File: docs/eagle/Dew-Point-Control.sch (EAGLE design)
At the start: 5 parts

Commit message: updated eagle board and schematic
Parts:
- added RELAYS: (no value), pinhead:PINHD-1X6
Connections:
- new net GPIO17: RELAYS.5, RPI_GPIO.11
- new net GPIO22: RELAYS.3, RPI_GPIO.15
- new net GPIO24: RELAYS.2, RPI_GPIO.18
- new net GPIO27: RELAYS.4, RPI_GPIO.13
- net 5V: now also RELAYS.6
- net GND: now also RELAYS.1
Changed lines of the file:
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@@
 <part name="R1" library="rcl" deviceset="R-EU_" device="0207/10" value="4,7K"/>
 <part name="R2" library="rcl" deviceset="R-EU_" device="0207/10" value="4,7K"/>
+<part name="RELAYS" library="pinhead" deviceset="PINHD-1X6" device=""/>
 </parts>
 <sheets>
@@
 <instance part="R1" gate="G$1" x="38.1" y="76.2" rot="R90"/>
 <instance part="R2" gate="G$1" x="63.5" y="76.2" rot="R90"/>
+<instance part="RELAYS" gate="A" x="83.82" y="48.26"/>
 </instances>
 <busses>
@@
 <wire x1="43.18" y1="83.82" x2="43.18" y2="73.66" width="0.1524" layer="91"/>
 <pinref part="SENSOR1" gate="A" pin="1"/>
-<wire x1="43.18" y1="73.66" x2="53.34" y2="73.66" width="0.1524" layer="91"/>
+<wire x1="43.18" y1="73.66" x2="45.72" y2="73.66" width="0.1524" layer="91"/>
+<wire x1="45.72" y1="73.66" x2="53.34" y2="73.66" width="0.1524" layer="91"/>
 <wire x1="43.18" y1="83.82" x2="63.5" y2="83.82" width="0.1524" layer="91"/>
 <wire x1="63.5" y1="83.82" x2="68.58" y2="83.82" width="0.1524" layer="91"/>
@@
 <junction x="43.18" y="83.82"/>
 <junction x="63.5" y="83.82"/>
+<wire x1="45.72" y1="73.66" x2="45.72" y2="43.18" width="0.1524" layer="91"/>
+<junction x="45.72" y="73.66"/>
+<pinref part="RELAYS" gate="A" pin="6"/>
+<wire x1="81.28" y1="43.18" x2="45.72" y2="43.18" width="0.1524" layer="91"/>
+<label x="71.12" y="43.18" size="1.778" layer="95"/>
 </segment>
 </net>
@@
 <label x="25.4" y="68.58" size="1.778" layer="95"/>
 <junction x="43.18" y="68.58"/>
+<wire x1="68.58" y1="60.96" x2="68.58" y2="55.88" width="0.1524" layer="91"/>
+<pinref part="RELAYS" gate="A" pin="1"/>
+<wire x1="68.58" y1="55.88" x2="81.28" y2="55.88" width="0.1524" layer="91"/>
+<junction x="68.58" y="60.96"/>
+<label x="71.12" y="55.88" size="1.778" layer="95"/>
 </segment>
 </net>
@@
 </segment>
 </net>
+<net name="GPIO24" class="0">
+<segment>
+<pinref part="RPI_GPIO" gate="A" pin="18"/>
+<label x="25.4" y="53.34" size="1.778" layer="95"/>
+<wire x1="20.32" y1="53.34" x2="81.28" y2="53.34" width="0.1524" layer="91"/>
+<pinref part="RELAYS" gate="A" pin="2"/>
+<label x="66.04" y="53.34" size="1.778" layer="95"/>
+</segment>
+</net>
+<net name="GPIO17" class="0">
+<segment>
+<pinref part="RPI_GPIO" gate="A" pin="11"/>
+<wire x1="12.7" y1="60.96" x2="-10.16" y2="60.96" width="0.1524" layer="91"/>
+<label x="-2.54" y="60.96" size="1.778" layer="95"/>
+<wire x1="-10.16" y1="60.96" x2="-10.16" y2="40.64" width="0.1524" layer="91"/>
+<wire x1="-10.16" y1="40.64" x2="38.1" y2="40.64" width="0.1524" layer="91"/>
+<wire x1="38.1" y1="40.64" x2="38.1" y2="45.72" width="0.1524" layer="91"/>
+<pinref part="RELAYS" gate="A" pin="5"/>
+<wire x1="38.1" y1="45.72" x2="81.28" y2="45.72" width="0.1524" layer="91"/>
+<label x="66.04" y="45.72" size="1.778" layer="95"/>
+</segment>
+</net>
+<net name="GPIO27" class="0">
+<segment>
+<pinref part="RPI_GPIO" gate="A" pin="13"/>
+<wire x1="12.7" y1="58.42" x2="-7.62" y2="58.42" width="0.1524" layer="91"/>
+<label x="-2.54" y="58.42" size="1.778" layer="95"/>
+<wire x1="-7.62" y1="58.42" x2="-7.62" y2="43.18" width="0.1524" layer="91"/>
+<wire x1="-7.62" y1="43.18" x2="35.56" y2="43.18" width="0.1524" layer="91"/>
+<wire x1="35.56" y1="43.18" x2="35.56" y2="48.26" width="0.1524" layer="91"/>
+<pinref part="RELAYS" gate="A" pin="4"/>
+<wire x1="35.56" y1="48.26" x2="81.28" y2="48.26" width="0.1524" layer="91"/>
+<label x="66.04" y="48.26" size="1.778" layer="95"/>
+</segment>
+</net>
+<net name="GPIO22" class="0">
+<segment>
+<pinref part="RPI_GPIO" gate="A" pin="15"/>
+<wire x1="12.7" y1="55.88" x2="-5.08" y2="55.88" width="0.1524" layer="91"/>
+<label x="-2.54" y="55.88" size="1.778" layer="95"/>
+<wire x1="-5.08" y1="55.88" x2="-5.08" y2="45.72" width="0.1524" layer="91"/>
+<wire x1="-5.08" y1="45.72" x2="33.02" y2="45.72" width="0.1524" layer="91"/>
+<wire x1="33.02" y1="45.72" x2="33.02" y2="50.8" width="0.1524" layer="91"/>
+<pinref part="RELAYS" gate="A" pin="3"/>
+<wire x1="33.02" y1="50.8" x2="81.28" y2="50.8" width="0.1524" layer="91"/>
+<label x="66.04" y="50.8" size="1.778" layer="95"/>
+</segment>
+</net>

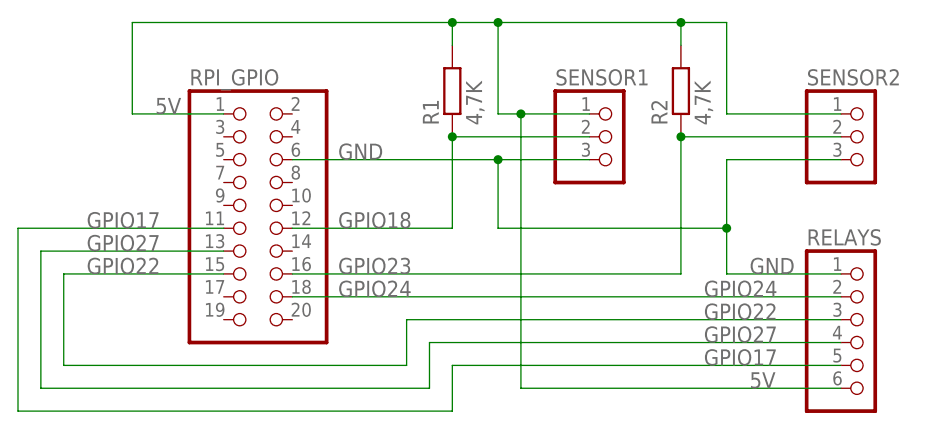
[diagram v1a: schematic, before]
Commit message: rename project and add init script
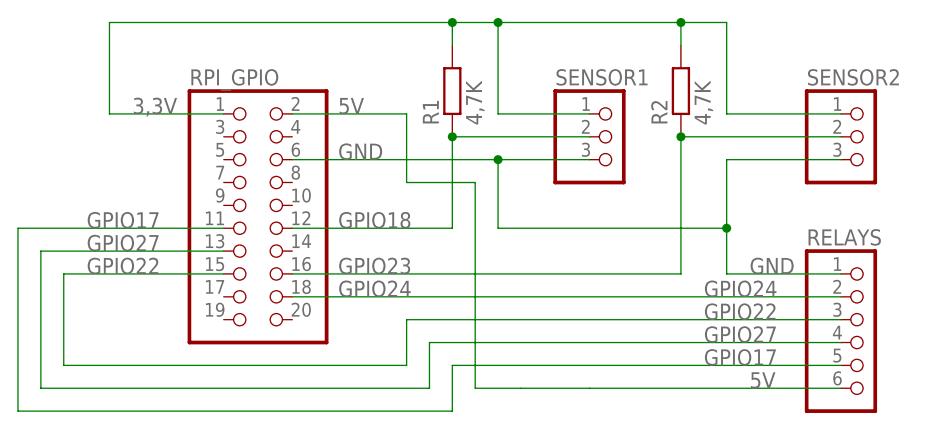
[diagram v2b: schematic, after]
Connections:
- new net 3,3V: R1.2, R2.2, RPI_GPIO.1, SENSOR1.1, SENSOR2.1
- net 5V: now also RPI_GPIO.2; no longer R1.2, R2.2, RPI_GPIO.1, SENSOR1.1, SENSOR2.1
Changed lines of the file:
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@@
 </busses>
 <nets>
-<net name="5V" class="0">
+<net name="3,3V" class="0">
 <segment>
 <pinref part="RPI_GPIO" gate="A" pin="1"/>
-<wire x1="12.7" y1="73.66" x2="2.54" y2="73.66" width="0.1524" layer="91"/>
-<wire x1="2.54" y1="73.66" x2="2.54" y2="83.82" width="0.1524" layer="91"/>
-<wire x1="2.54" y1="83.82" x2="38.1" y2="83.82" width="0.1524" layer="91"/>
+<wire x1="12.7" y1="73.66" x2="0" y2="73.66" width="0.1524" layer="91"/>
+<wire x1="0" y1="73.66" x2="0" y2="83.82" width="0.1524" layer="91"/>
+<wire x1="0" y1="83.82" x2="38.1" y2="83.82" width="0.1524" layer="91"/>
 <wire x1="38.1" y1="83.82" x2="43.18" y2="83.82" width="0.1524" layer="91"/>
 <wire x1="43.18" y1="83.82" x2="43.18" y2="73.66" width="0.1524" layer="91"/>
 <pinref part="SENSOR1" gate="A" pin="1"/>
-<wire x1="43.18" y1="73.66" x2="45.72" y2="73.66" width="0.1524" layer="91"/>
-<wire x1="45.72" y1="73.66" x2="53.34" y2="73.66" width="0.1524" layer="91"/>
+<wire x1="43.18" y1="73.66" x2="53.34" y2="73.66" width="0.1524" layer="91"/>
 <wire x1="43.18" y1="83.82" x2="63.5" y2="83.82" width="0.1524" layer="91"/>
 <wire x1="63.5" y1="83.82" x2="68.58" y2="83.82" width="0.1524" layer="91"/>
@@
 <pinref part="R2" gate="G$1" pin="2"/>
 <wire x1="63.5" y1="81.28" x2="63.5" y2="83.82" width="0.1524" layer="91"/>
-<label x="5.08" y="73.66" size="1.778" layer="95"/>
+<label x="2.54" y="73.66" size="1.778" layer="95"/>
 <junction x="38.1" y="83.82"/>
 <junction x="43.18" y="83.82"/>
 <junction x="63.5" y="83.82"/>
-<wire x1="45.72" y1="73.66" x2="45.72" y2="43.18" width="0.1524" layer="91"/>
-<junction x="45.72" y="73.66"/>
-<pinref part="RELAYS" gate="A" pin="6"/>
-<wire x1="81.28" y1="43.18" x2="45.72" y2="43.18" width="0.1524" layer="91"/>
-<label x="71.12" y="43.18" size="1.778" layer="95"/>
 </segment>
 </net>
@@
 </segment>
 </net>
+<net name="5V" class="0">
+<segment>
+<pinref part="RPI_GPIO" gate="A" pin="2"/>
+<wire x1="20.32" y1="73.66" x2="33.02" y2="73.66" width="0.1524" layer="91"/>
+<wire x1="33.02" y1="73.66" x2="33.02" y2="66.04" width="0.1524" layer="91"/>
+<wire x1="33.02" y1="66.04" x2="40.64" y2="66.04" width="0.1524" layer="91"/>
+<wire x1="40.64" y1="66.04" x2="40.64" y2="43.18" width="0.1524" layer="91"/>
+<pinref part="RELAYS" gate="A" pin="6"/>
+<wire x1="81.28" y1="43.18" x2="53.34" y2="43.18" width="0.1524" layer="91"/>
+<label x="71.12" y="43.18" size="1.778" layer="95"/>
+<wire x1="45.72" y1="43.18" x2="40.64" y2="43.18" width="0.1524" layer="91"/>
+<wire x1="45.72" y1="43.18" x2="53.34" y2="43.18" width="0.1524" layer="91"/>
+<label x="25.4" y="73.66" size="1.778" layer="95"/>
+</segment>
+</net>
